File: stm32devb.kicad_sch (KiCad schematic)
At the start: 60 parts, among them IC1 TJA1441AT_0Z, J1 USB_C_Receptacle_USB2.0, J2 SPI1, J3 SPI2, J4 I2C1, J5 I2C2, J6 Conn_01x04, J7 Conn_01x04, J8 Conn_01x02, J9 Conn_01x02, Q1 BSS138, Q2 BSS138, SW1 EN0, SW2 BOOT0, U1 ESP32-WROOM-32, U2 FT232RL, U3 XT60PW-M, U4 ADP3338AKCZ-3.3, U5 XT30PW-M, U6 XT30PW-M, U7 XT30PW-M

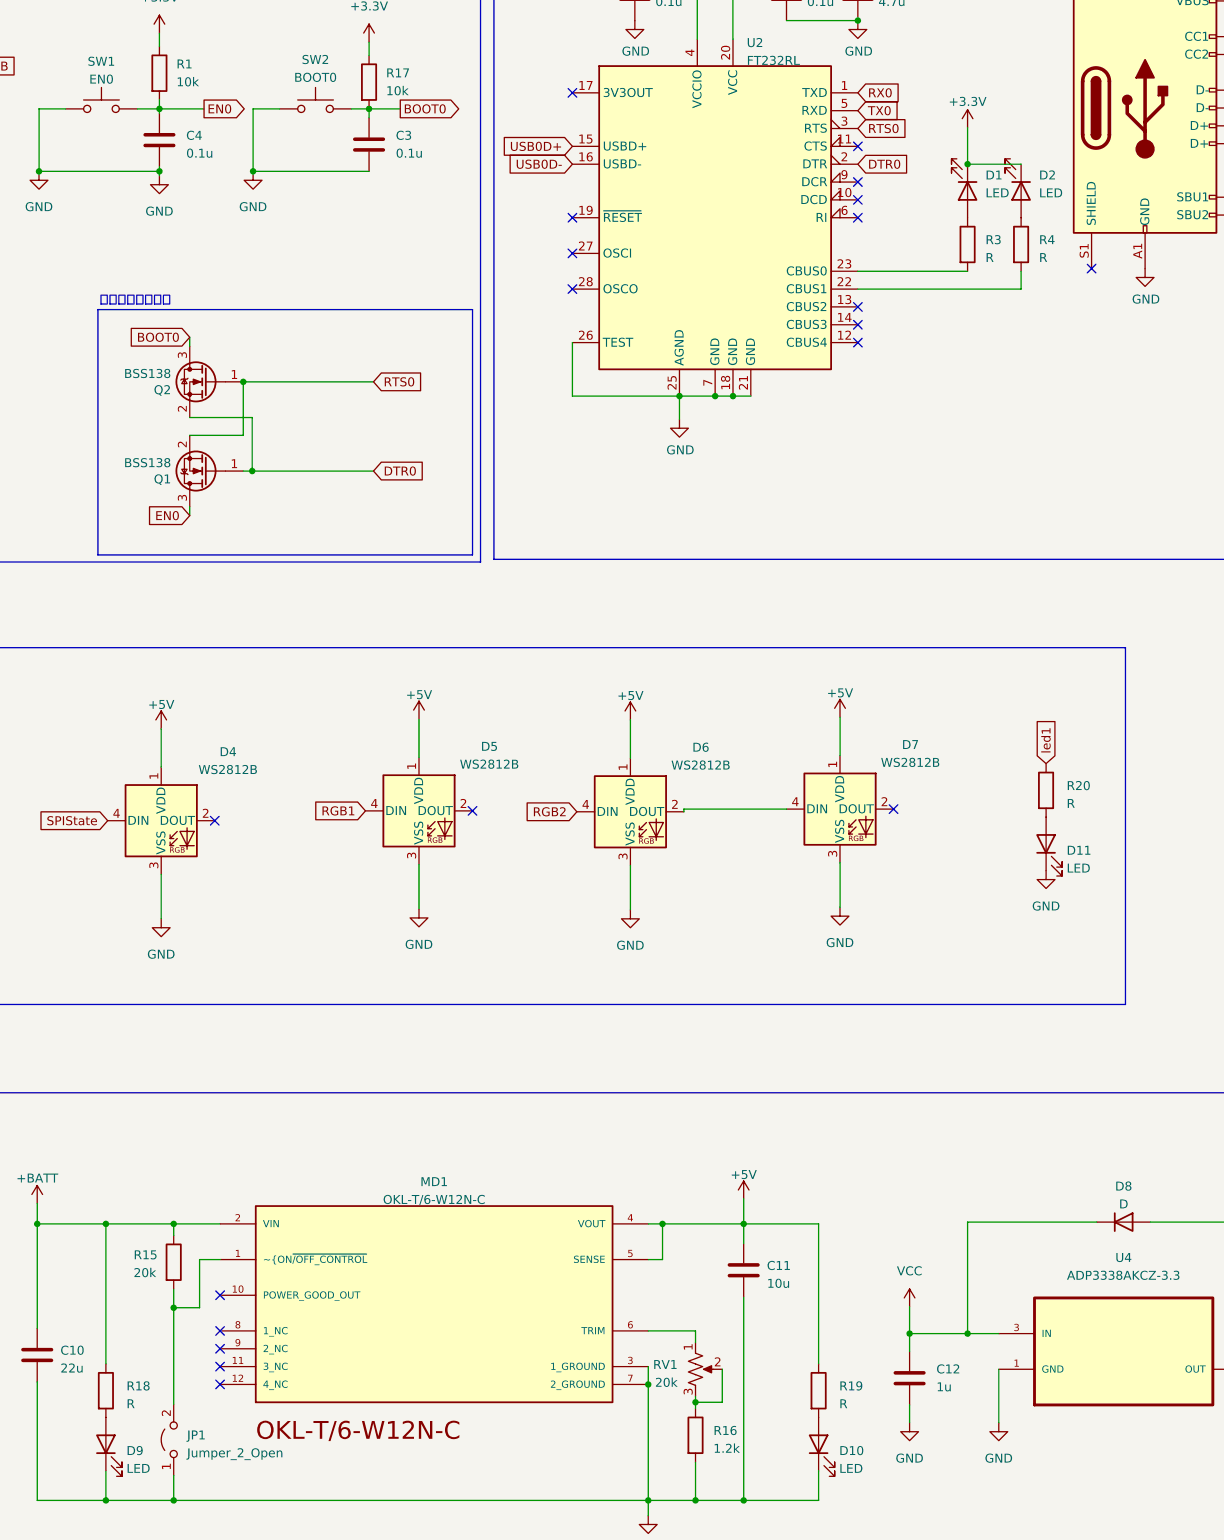
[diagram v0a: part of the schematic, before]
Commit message: ENのコンデンサーを1uFにしました
自動起動と自動書き込みの為です。
今回実装した抵抗器の値を入れておきました
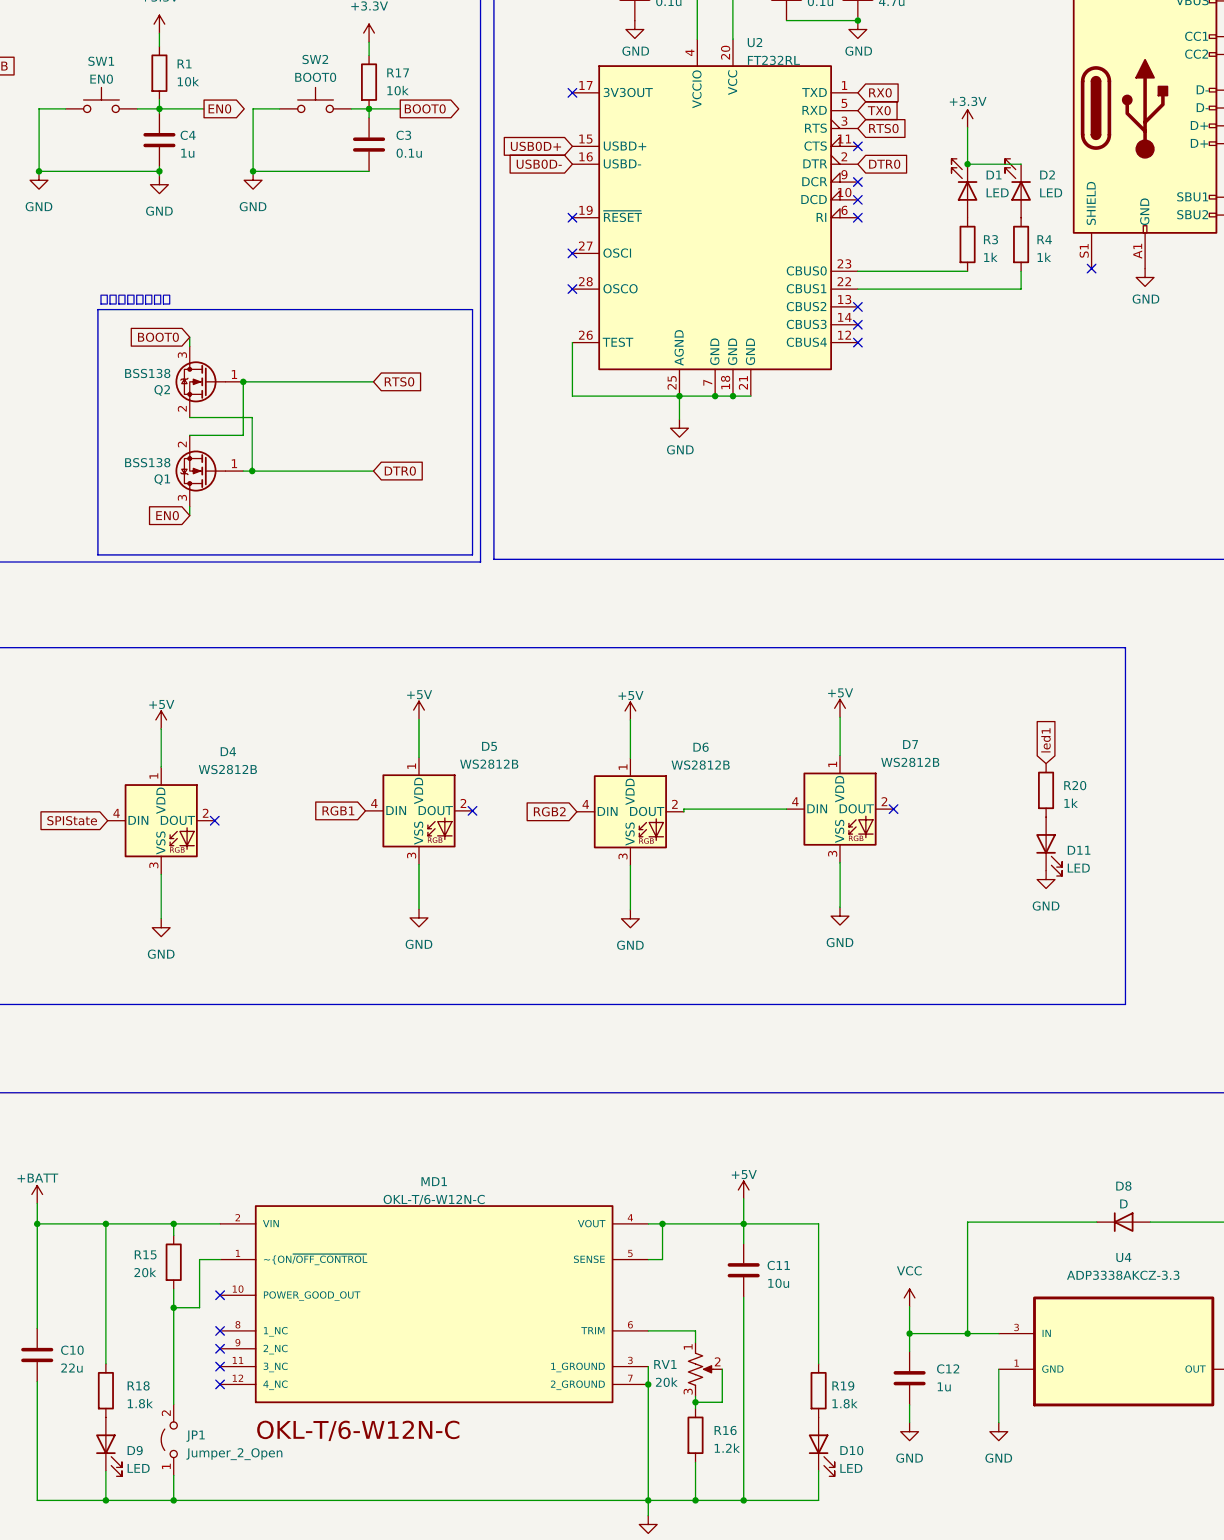
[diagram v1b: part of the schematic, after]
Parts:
- C4: value 0.1u -> 1u
- R18, R19: value R -> 1.8k
- R20, R3, R4: value R -> 1k
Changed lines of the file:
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@@
   (symbol (lib_id "Device:R") (at 219.837 165.735 0) (unit 1)
     (in_bom yes) (on_board yes) (dnp no) (fields_autoplaced)
-    (property "Reference" "R20" (at 222.758 165.1 0)
-      (effects (font (size 1.27 1.27)) (justify left))
-    )
-    (property "Value" "R" (at 222.758 167.64 0)
+    (property "Reference" "R20" (at 222.25 165.1 0)
+      (effects (font (size 1.27 1.27)) (justify left))
+    )
+    (property "Value" "1k" (at 222.25 167.64 0)
       (effects (font (size 1.27 1.27)) (justify left))
     )
@@
       (effects (font (size 1.27 1.27)) (justify left))
     )
-    (property "Value" "R" (at 88.9 253.111 0)
+    (property "Value" "1.8k" (at 88.9 253.111 0)
       (effects (font (size 1.27 1.27)) (justify left))
     )
@@
   (symbol (lib_id "Device:C") (at 93.599 73.152 0) (unit 1)
     (in_bom yes) (on_board yes) (dnp no) (fields_autoplaced)
-    (property "Reference" "C4" (at 97.409 72.517 0)
-      (effects (font (size 1.27 1.27)) (justify left))
-    )
-    (property "Value" "0.1u" (at 97.409 75.057 0)
+    (property "Reference" "C4" (at 96.52 72.517 0)
+      (effects (font (size 1.27 1.27)) (justify left))
+    )
+    (property "Value" "1u" (at 96.52 75.057 0)
       (effects (font (size 1.27 1.27)) (justify left))
     )
@@
   (symbol (lib_id "Device:R") (at 187.452 251.206 0) (unit 1)
     (in_bom yes) (on_board yes) (dnp no) (fields_autoplaced)
-    (property "Reference" "R19" (at 190.373 250.571 0)
-      (effects (font (size 1.27 1.27)) (justify left))
-    )
-    (property "Value" "R" (at 190.373 253.111 0)
+    (property "Reference" "R19" (at 189.23 250.571 0)
+      (effects (font (size 1.27 1.27)) (justify left))
+    )
+    (property "Value" "1.8k" (at 189.23 253.111 0)
       (effects (font (size 1.27 1.27)) (justify left))
     )
@@
   (symbol (lib_id "Device:R") (at 208.661 88.011 0) (unit 1)
     (in_bom yes) (on_board yes) (dnp no) (fields_autoplaced)
-    (property "Reference" "R3" (at 211.201 87.376 0)
-      (effects (font (size 1.27 1.27)) (justify left))
-    )
-    (property "Value" "R" (at 211.201 89.916 0)
+    (property "Reference" "R3" (at 210.82 87.376 0)
+      (effects (font (size 1.27 1.27)) (justify left))
+    )
+    (property "Value" "1k" (at 210.82 89.916 0)
       (effects (font (size 1.27 1.27)) (justify left))
     )
@@
   (symbol (lib_id "Device:R") (at 216.281 88.011 0) (unit 1)
     (in_bom yes) (on_board yes) (dnp no) (fields_autoplaced)
-    (property "Reference" "R4" (at 218.821 87.376 0)
-      (effects (font (size 1.27 1.27)) (justify left))
-    )
-    (property "Value" "R" (at 218.821 89.916 0)
-      (effects (font (size 1.27 1.27)) (justify left))
-    )
+    (property "Reference" "R4" (at 218.44 87.376 0)
+      (effects (font (size 1.27 1.27)) (justify left))
+    )
+    (property "Value" "1k" (at 218.44 89.916 0)
+      (effects (font (size 1.27 1.27)) (justify left))
+    )
